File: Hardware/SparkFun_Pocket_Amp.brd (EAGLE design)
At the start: 91.4 x 55.9 mm, 54 parts, among them J1 AUDIO_JACK, J2 AUDIO_JACK, J3 micro USB, U1 LM4853, U2 LM358, U3 TPS61200, U4 MCP73831

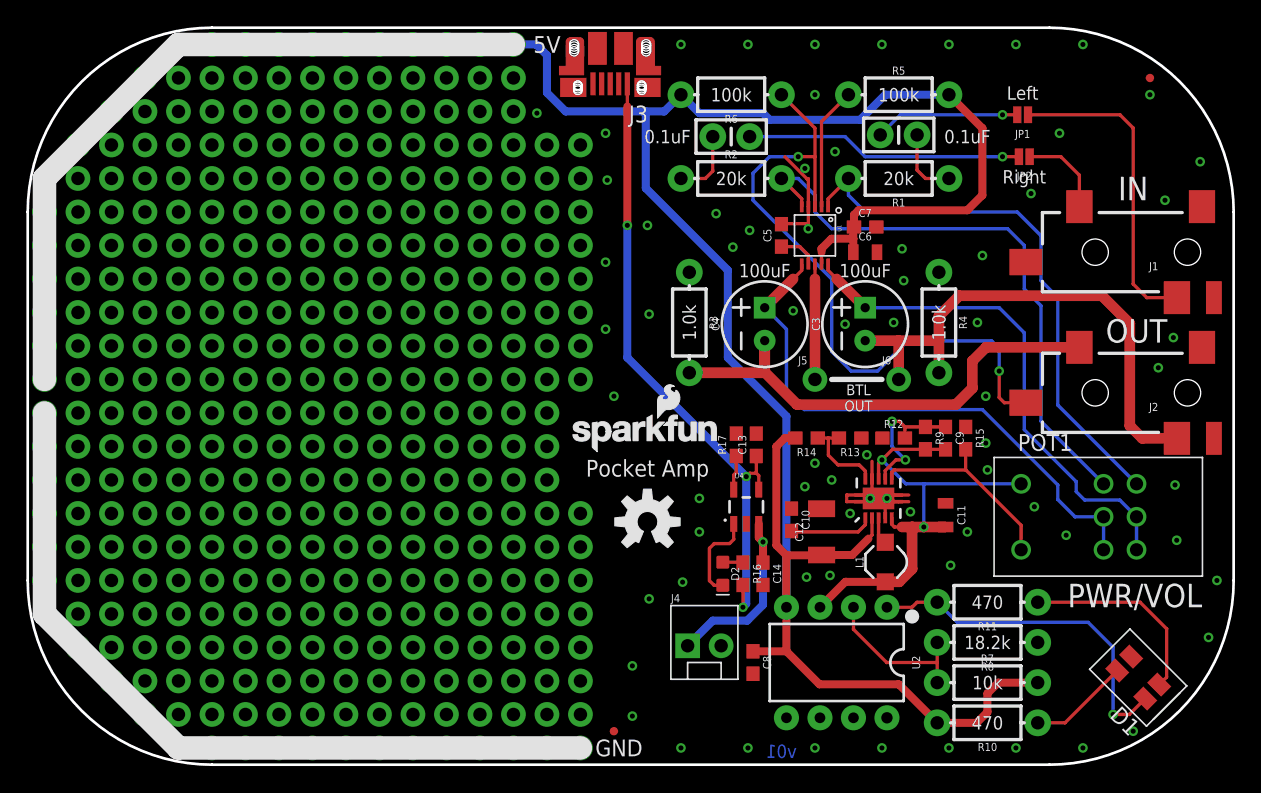
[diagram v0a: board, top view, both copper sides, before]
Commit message: Added PROD_ID to C12
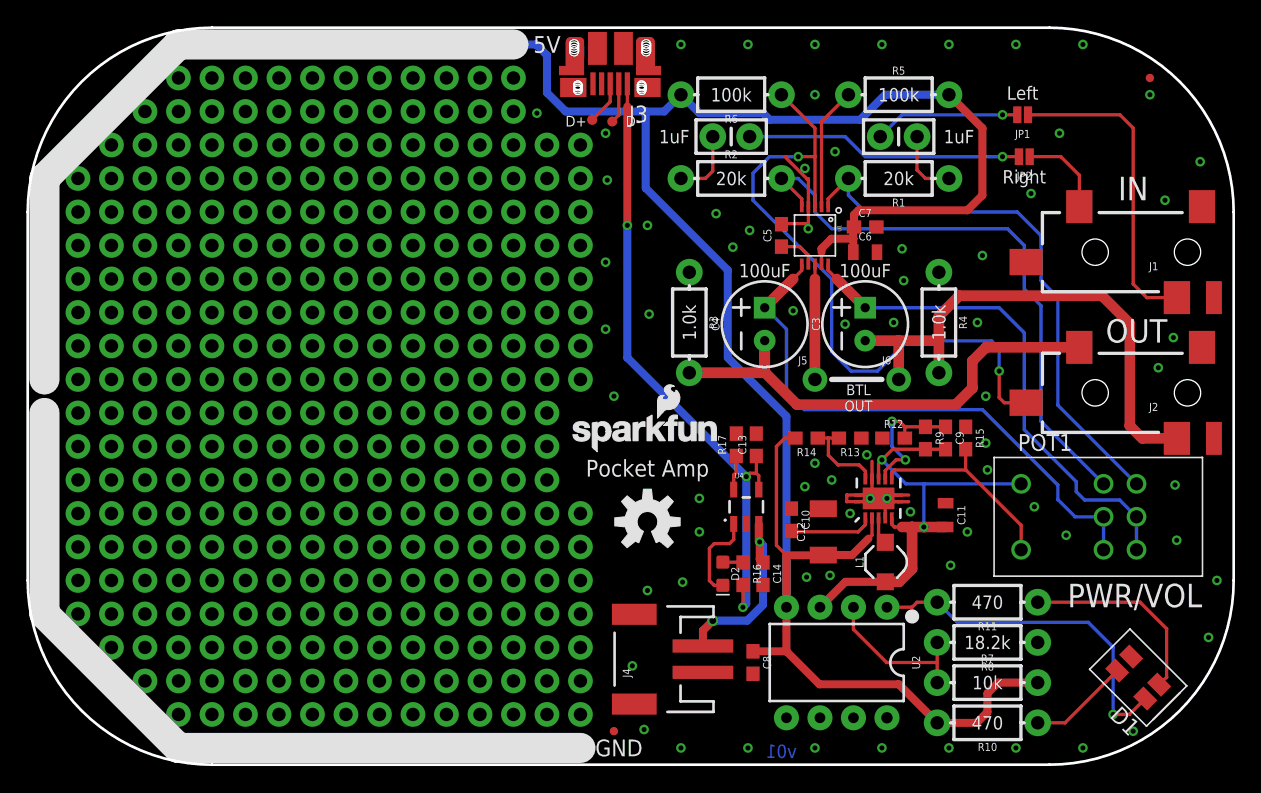
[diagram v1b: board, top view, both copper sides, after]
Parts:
- added TP1, TP2: (no value), SparkFun-Connectors:PAD.03X.03
- C12: value 22UF -> 22uF
- J4: device SparkFun-Connectors:MOLEX-1X2 -> SparkFun-Connectors:JST-2-SMD
- moved J4 2.74 mm to (47.5, 8.00), turned to 90 degrees
- moved C1 0.13 mm to (66.0, 47.6)
- moved C12 0.13 mm to (60.3, 17.7)
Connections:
- new net N$10: J3.D-, TP1.P$1
- new net N$18: J3.D+, TP2.P$1
- net GND: now also J4.1; no longer J4.2
- net N$22: now also J4.2; no longer J4.1
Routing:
- net N$18: track 0.00 -> 3.30 mm
- net N$10: track 0.00 -> 3.06 mm
- net N$22: track 14.8 -> 14.5 mm, vias 1 -> 2
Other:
- board text added: "1uF"
- board text added: "D+"
- board text added: "D-"
- board text removed: "0.1uF"

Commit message: DFM Changes
Added values missing on a few parts
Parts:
- D1: value (none) -> LED Inicator
- J4: value (none) -> Battery Conn.
- POT1: value (none) -> 20k
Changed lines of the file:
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@@
 <setting verticaltext="up"/>
 </settings>
-<grid distance="0.05" unitdist="inch" unit="inch" style="lines" multiple="1" display="yes" altdistance="0.005" altunitdist="inch" altunit="inch"/>
+<grid distance="0.001" unitdist="inch" unit="inch" style="lines" multiple="1" display="yes" altdistance="0.01" altunitdist="inch" altunit="inch"/>
 <layers>
-<layer number="1" name="Top" color="4" fill="1" visible="yes" active="yes"/>
+<layer number="1" name="Top" color="4" fill="1" visible="no" active="yes"/>
 <layer number="2" name="Route2" color="1" fill="3" visible="no" active="no"/>
 <layer number="3" name="Route3" color="4" fill="3" visible="no" active="no"/>
@@
 <layer number="14" name="Route14" color="1" fill="6" visible="no" active="no"/>
 <layer number="15" name="Route15" color="4" fill="6" visible="no" active="no"/>
-<layer number="16" name="Bottom" color="1" fill="1" visible="yes" active="yes"/>
+<layer number="16" name="Bottom" color="1" fill="1" visible="no" active="yes"/>
 <layer number="17" name="Pads" color="2" fill="1" visible="yes" active="yes"/>
-<layer number="18" name="Vias" color="2" fill="1" visible="yes" active="yes"/>
-<layer number="19" name="Unrouted" color="6" fill="1" visible="yes" active="yes"/>
+<layer number="18" name="Vias" color="2" fill="1" visible="no" active="yes"/>
+<layer number="19" name="Unrouted" color="6" fill="1" visible="no" active="yes"/>
 <layer number="20" name="Dimension" color="15" fill="1" visible="yes" active="yes"/>
 <layer number="21" name="tPlace" color="16" fill="1" visible="yes" active="yes"/>
-<layer number="22" name="bPlace" color="14" fill="1" visible="yes" active="yes"/>
+<layer number="22" name="bPlace" color="14" fill="1" visible="no" active="yes"/>
 <layer number="23" name="tOrigins" color="15" fill="1" visible="yes" active="yes"/>
-<layer number="24" name="bOrigins" color="15" fill="1" visible="yes" active="yes"/>
+<layer number="24" name="bOrigins" color="15" fill="1" visible="no" active="yes"/>
 <layer number="25" name="tNames" color="7" fill="1" visible="no" active="yes"/>
 <layer number="26" name="bNames" color="7" fill="1" visible="no" active="yes"/>
-<layer number="27" name="tValues" color="7" fill="1" visible="no" active="yes"/>
+<layer number="27" name="tValues" color="7" fill="1" visible="yes" active="yes"/>
 <layer number="28" name="bValues" color="7" fill="1" visible="no" active="yes"/>
 <layer number="29" name="tStop" color="7" fill="3" visible="no" active="yes"/>
 <layer number="30" name="bStop" color="7" fill="6" visible="no" active="yes"/>
-<layer number="31" name="tCream" color="7" fill="4" visible="no" active="yes"/>
+<layer number="31" name="tCream" color="7" fill="4" visible="yes" active="yes"/>
 <layer number="32" name="bCream" color="7" fill="5" visible="no" active="yes"/>
 <layer number="33" name="tFinish" color="6" fill="3" visible="no" active="yes"/>
@@
 <attribute name="PROD_ID" value=" " x="53.34" y="50.8" size="1.778" layer="27" font="vector" ratio="15" rot="R180" display="off"/>
 </element>
-<element name="POT1" library="SparkFun-Resistors" package="POT-DUAL-SWITCH-PTH" value="" x="84.074" y="18.796"/>
+<element name="POT1" library="SparkFun-Resistors" package="POT-DUAL-SWITCH-PTH" value="20k" x="84.074" y="18.796"/>
 <element name="C5" library="SparkFun-Capacitors" package="0603" value="1.0uF" x="57.15" y="40.132" rot="R90">
 <attribute name="PROD_ID" value="CAP-00868" x="57.15" y="40.132" size="1.778" layer="27" font="vector" ratio="15" rot="R90" display="off"/>
@@
 <attribute name="PROD_ID" value=" " x="72.771" y="12.319" size="1.778" layer="27" font="vector" ratio="15" rot="R180" display="off"/>
 </element>
-<element name="D1" library="SparkFun-LED" package="LED_3MM_RG_SMD" value="" x="84.201" y="6.604" rot="R135"/>
+<element name="D1" library="SparkFun-LED" package="LED_3MM_RG_SMD" value="LED Inicator" x="84.201" y="6.604" rot="R135"/>
 <element name="U2" library="SparkFun-IC-Amplifiers" package="DIP08-KIT" value="LM358" x="61.341" y="7.747" rot="R180">
 <attribute name="PROD_ID" value="IC-09172" x="61.341" y="7.747" size="1.778" layer="27" font="vector" ratio="15" rot="R180" display="off"/>
@@
 <attribute name="PROD_ID" value="CONN-13711" x="44.196" y="52.959" size="1.016" layer="27" font="vector" ratio="15" rot="R180" display="off"/>
 </element>
-<element name="J4" library="SparkFun-Connectors" package="JST-2-SMD" value="" x="47.498" y="8.001" rot="R90">
+<element name="J4" library="SparkFun-Connectors" package="JST-2-SMD" value="Battery Conn." x="47.498" y="8.001" rot="R90">
 <attribute name="PROD_ID" value="CONN-11443" x="47.498" y="8.001" size="1.778" layer="27" rot="R90" display="off"/>
 </element>
